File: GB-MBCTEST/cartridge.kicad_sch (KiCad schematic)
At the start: 11 parts

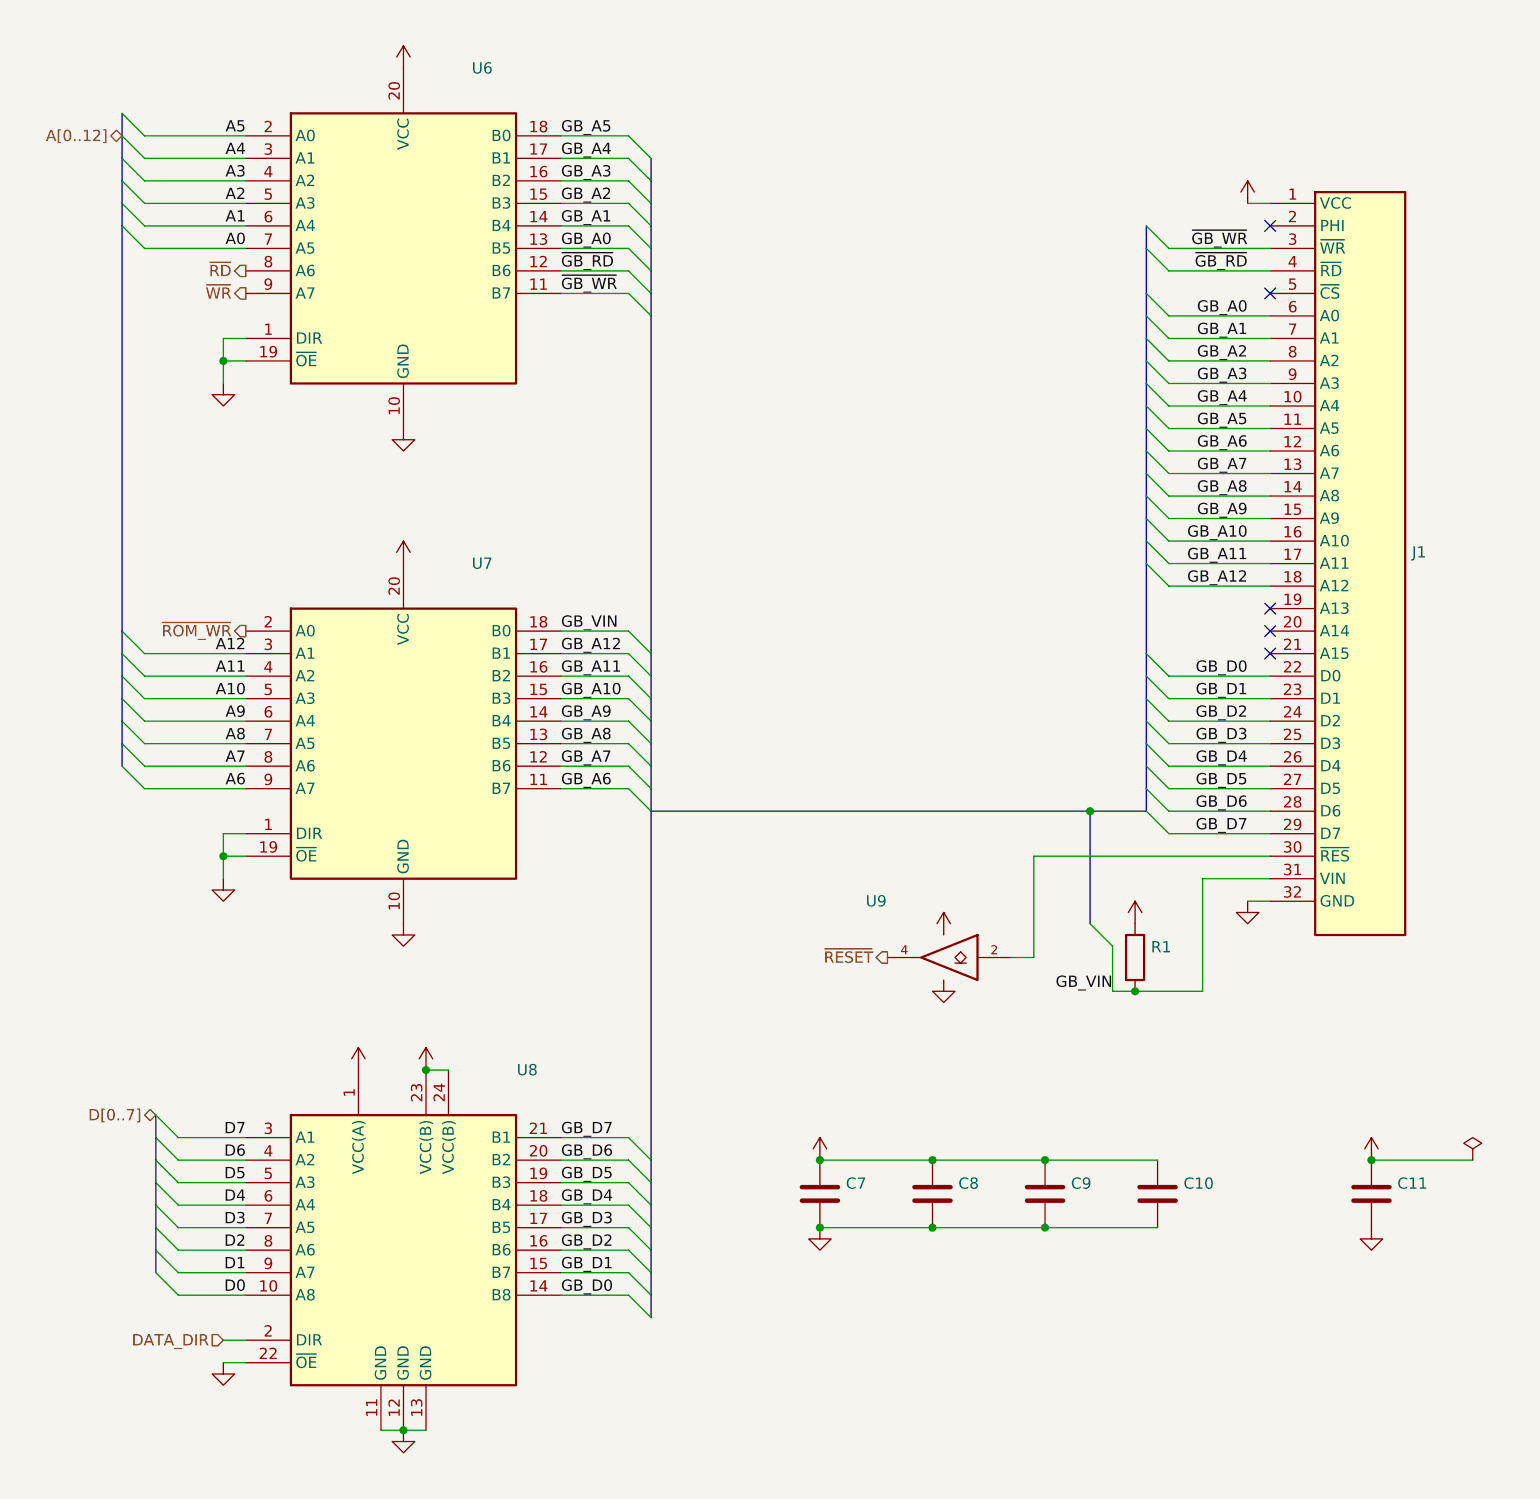
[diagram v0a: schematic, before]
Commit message: Upgrade projects to KiCad 7
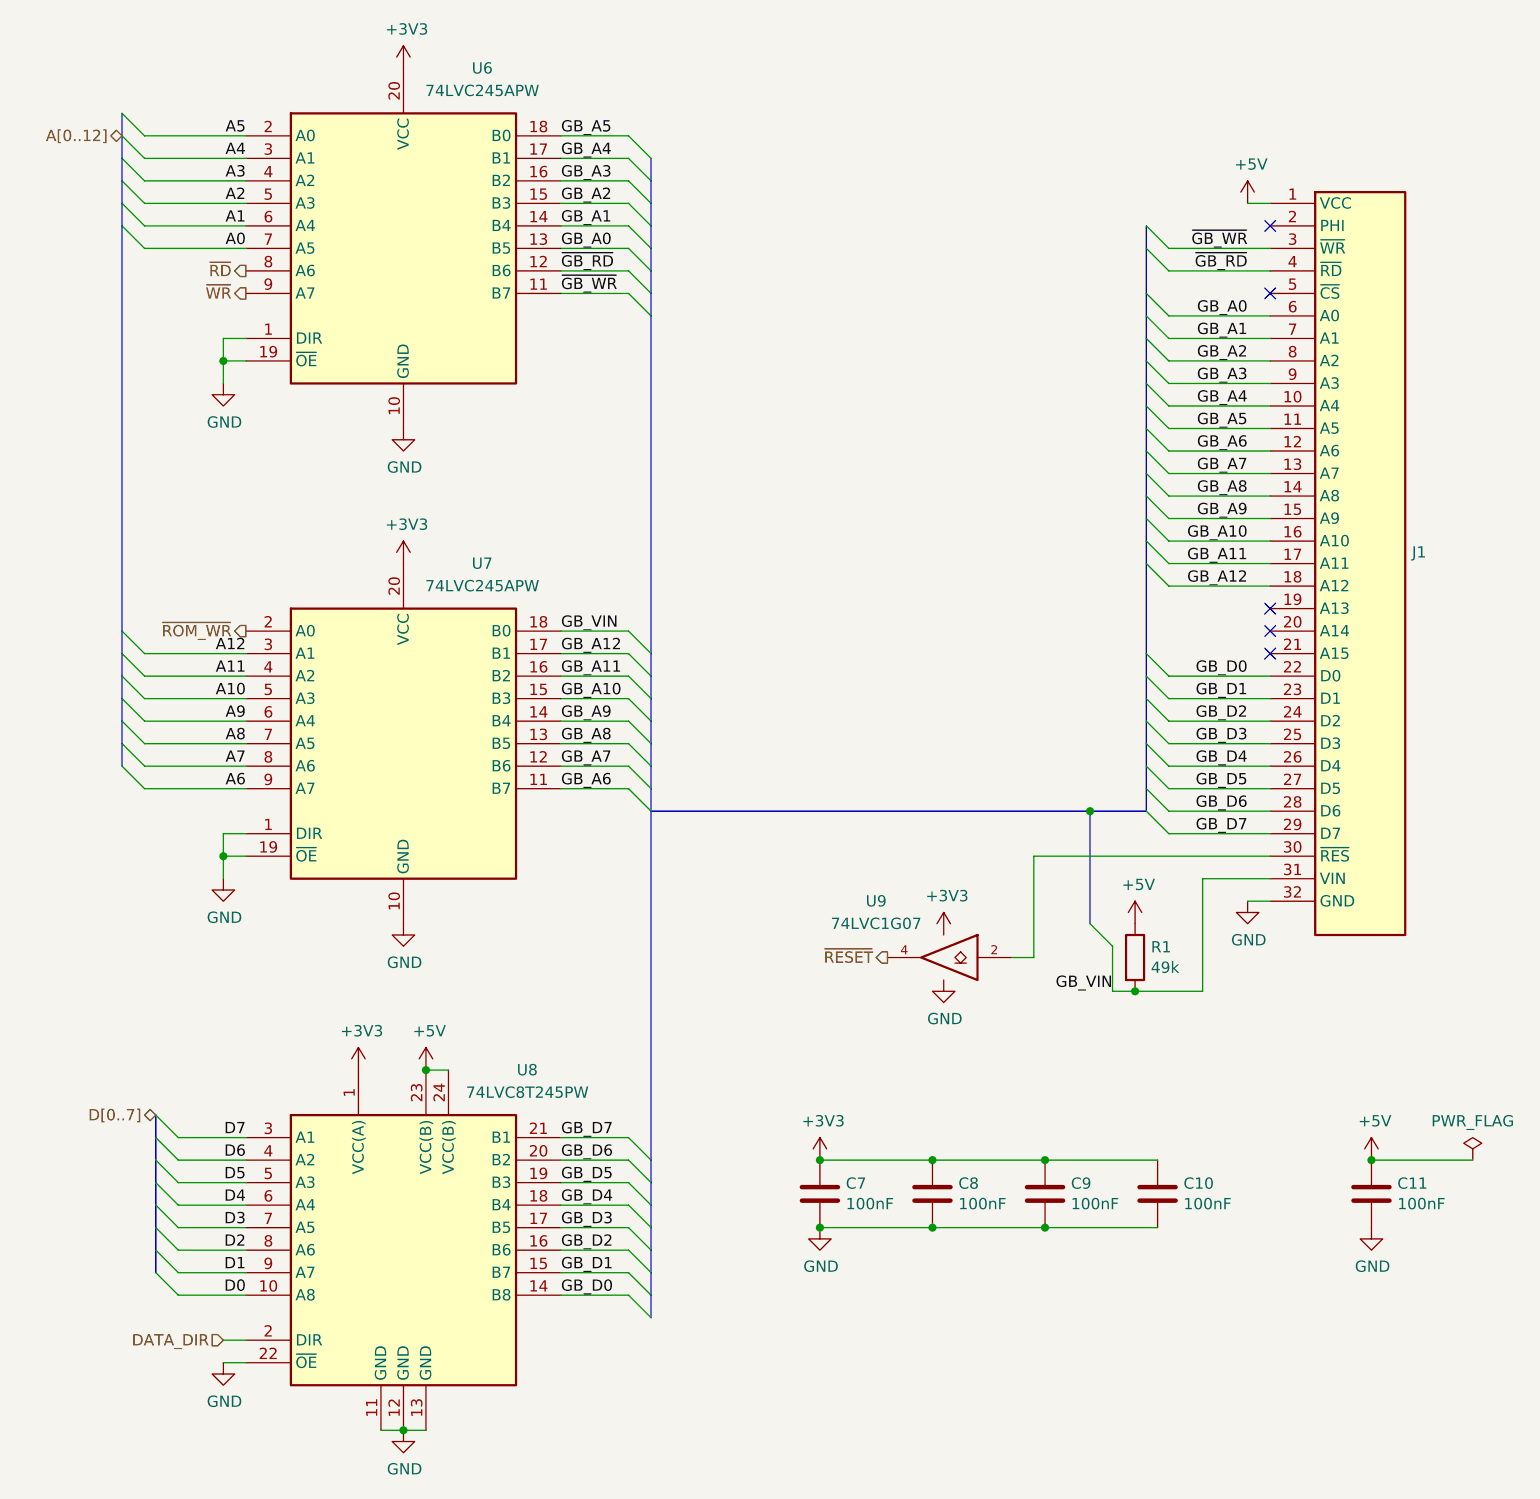
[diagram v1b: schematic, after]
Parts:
- C10, C11, C7, C8, C9: value (none) -> 100nF; footprint (none) -> Capacitor_SMD:C_0603_1608Metric
- J1: value (none) -> DNF; footprint (none) -> Gekkio_Connector_PCBEdge:GameBoy_Cartridge_1x32_P1.50mm_Edge
- R1: value (none) -> 49k; footprint (none) -> Resistor_SMD:R_0603_1608Metric
- U6, U7: value (none) -> 74LVC245APW; footprint (none) -> Package_SO:TSSOP-20_4.4x6.5mm_P0.65mm
- U8: value (none) -> 74LVC8T245PW; footprint (none) -> Package_SO:TSSOP-24_4.4x7.8mm_P0.65mm
- U9: value (none) -> 74LVC1G07; footprint (none) -> Package_TO_SOT_SMD:SOT-353_SC-70-5
